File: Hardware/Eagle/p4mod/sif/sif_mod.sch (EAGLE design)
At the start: 29 parts

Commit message: Lowered values of the segment resistors for the Sif board.
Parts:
- R2, R3, R4, R5, R6, R7, R8: value 82 -> 75
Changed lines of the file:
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@@
 <part name="SUPPLY2" library="supply2" deviceset="GND" device=""/>
 <part name="SUPPLY3" library="supply2" deviceset="GND" device=""/>
-<part name="R2" library="resistor_mod" deviceset="R-EU_" device="R0402" value="82"/>
-<part name="R3" library="resistor_mod" deviceset="R-EU_" device="R0402" value="82"/>
-<part name="R4" library="resistor_mod" deviceset="R-EU_" device="R0402" value="82"/>
-<part name="R5" library="resistor_mod" deviceset="R-EU_" device="R0402" value="82"/>
-<part name="R6" library="resistor_mod" deviceset="R-EU_" device="R0402" value="82"/>
-<part name="R7" library="resistor_mod" deviceset="R-EU_" device="R0402" value="82"/>
-<part name="R8" library="resistor_mod" deviceset="R-EU_" device="R0402" value="82"/>
+<part name="R2" library="resistor_mod" deviceset="R-EU_" device="R0402" value="75"/>
+<part name="R3" library="resistor_mod" deviceset="R-EU_" device="R0402" value="75"/>
+<part name="R4" library="resistor_mod" deviceset="R-EU_" device="R0402" value="75"/>
+<part name="R5" library="resistor_mod" deviceset="R-EU_" device="R0402" value="75"/>
+<part name="R6" library="resistor_mod" deviceset="R-EU_" device="R0402" value="75"/>
+<part name="R7" library="resistor_mod" deviceset="R-EU_" device="R0402" value="75"/>
+<part name="R8" library="resistor_mod" deviceset="R-EU_" device="R0402" value="75"/>
 <part name="FRAME1" library="frames" deviceset="A4-SMALL-DOCFIELD" device="" value="Pulsar P4 Replacement Module"/>
 <part name="C4" library="resistor_mod" deviceset="C-EU" device="C0402K" value="12 pF"/>

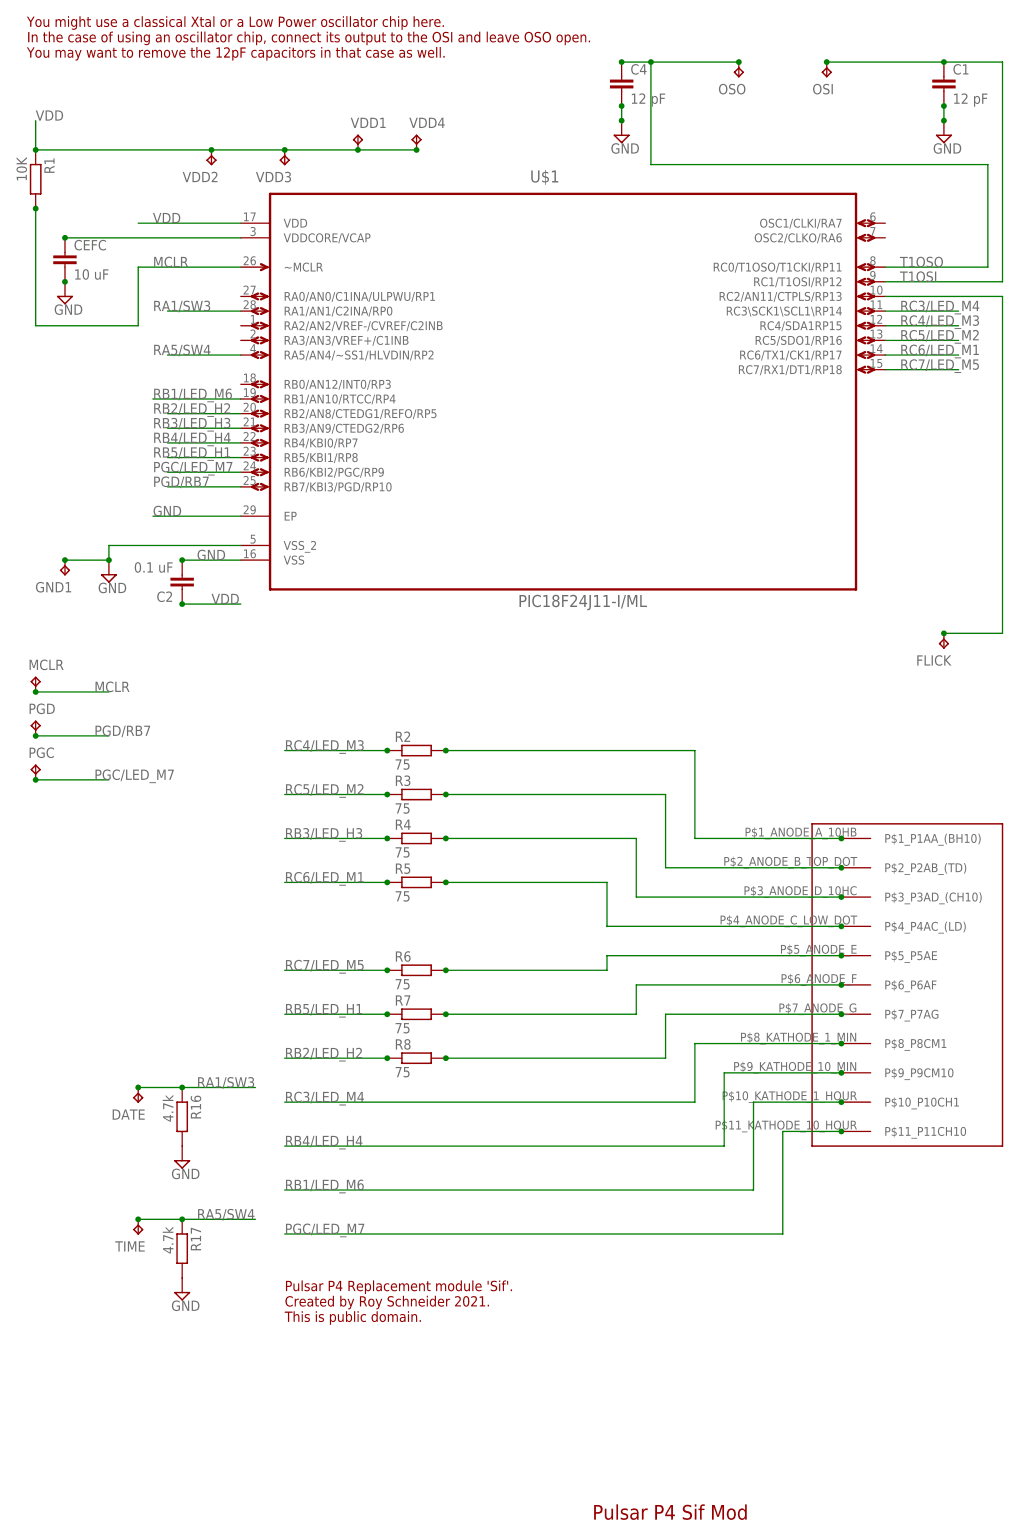
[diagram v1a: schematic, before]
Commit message: Upgraded Sif module to use nmos transistors for the common cathodes.
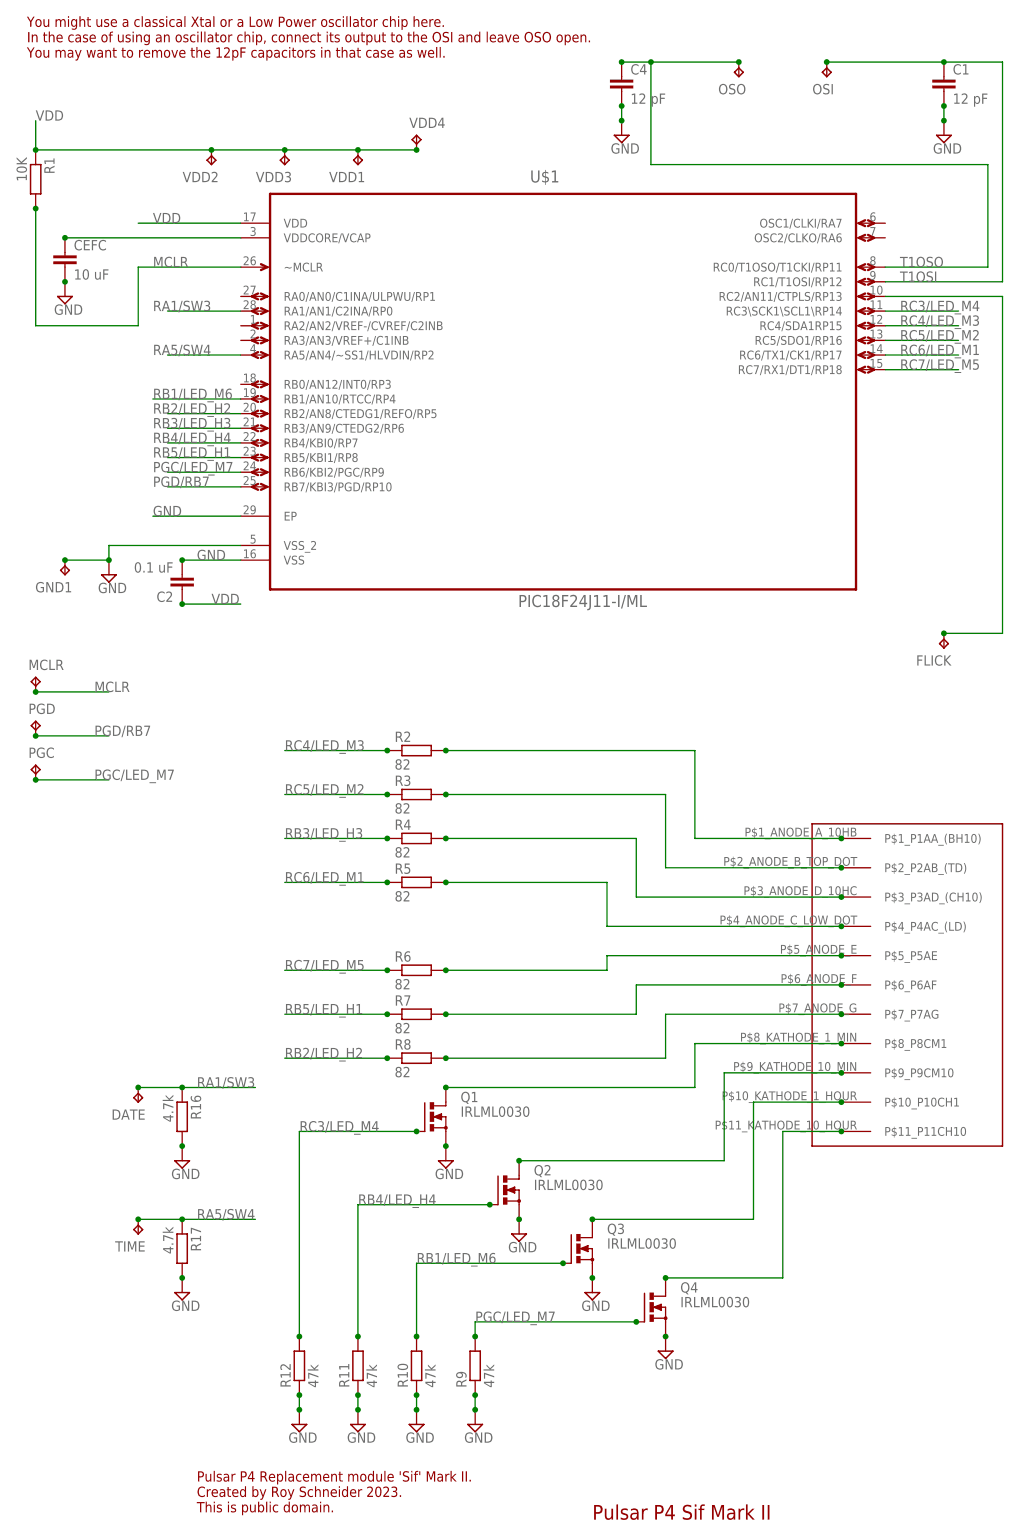
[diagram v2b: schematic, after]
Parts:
- added Q1, Q2, Q3, Q4: IRLML0030, irlml0030:IRLML0030
- added R10, R11, R12, R9: 47k, resistor_mod:R-EU_R0402
- R2, R3, R4, R5, R6, R7, R8: value 75 -> 82
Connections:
- new net N$11: Q2.D, U$2.P$9_P9CM10
- new net N$12: Q3.D, U$2.P$10_P10CH1
- new net N$13: Q4.D, U$2.P$11_P11CH10
- new net N$14: Q1.D, U$2.P$8_P8CM1
- net GND: now also Q1.S, Q2.S, Q3.S, Q4.S, R10.1, R11.1, R12.1, R9.1
- net PGC/LED_M7: now also Q4.G, R9.2; no longer U$2.P$11_P11CH10
- net RB1/LED_M6: now also Q3.G, R10.2; no longer U$2.P$10_P10CH1
- net RB4/LED_H4: now also Q2.G, R11.2; no longer U$2.P$9_P9CM10
- net RC3/LED_M4: now also Q1.G, R12.2; no longer U$2.P$8_P8CM1
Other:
- note added: "Pulsar P4 Replacement module 'Sif' Mark II. Created by Roy Schneider 2023. This is public domain."
- note added: "Pulsar P4 Sif Mark II"
- note removed: "Pulsar P4 Replacement module 'Sif'. Created by Roy Schneider 2021. This is public domain."
- note removed: "Pulsar P4 Sif Mod"
- moved on the sheet: VDD1

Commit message: Updated footprint of 10 uF ceramic cap to 0602.
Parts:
- CEFC: device resistor_mod:C-EUC0402K -> rcl:C-EUC0603
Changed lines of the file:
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@@
 <part name="R1" library="resistor_mod" deviceset="R-EU_" device="R0402" value="10K"/>
 <part name="C2" library="resistor_mod" deviceset="C-EU" device="C0402K" value="0.1 uF"/>
-<part name="CEFC" library="resistor_mod" deviceset="C-EU" device="C0402K" value="10 uF"/>
+<part name="CEFC" library="rcl" deviceset="C-EU" device="C0603" value="10 uF"/>
 <part name="SUPPLY2" library="supply2" deviceset="GND" device=""/>
 <part name="SUPPLY3" library="supply2" deviceset="GND" device=""/>

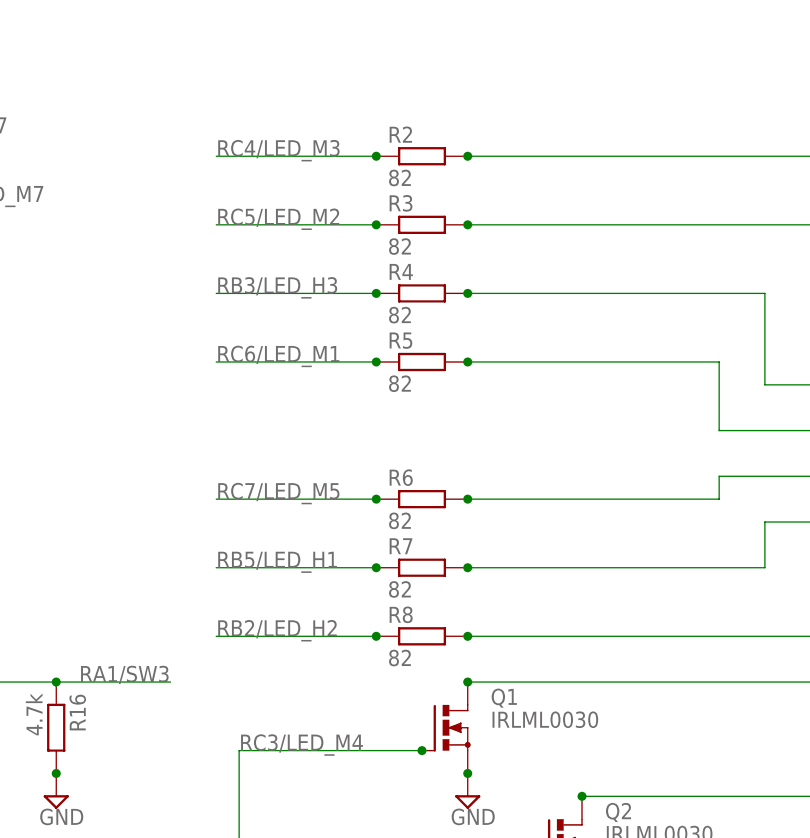
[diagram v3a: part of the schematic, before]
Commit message: Improved segment resistor values.
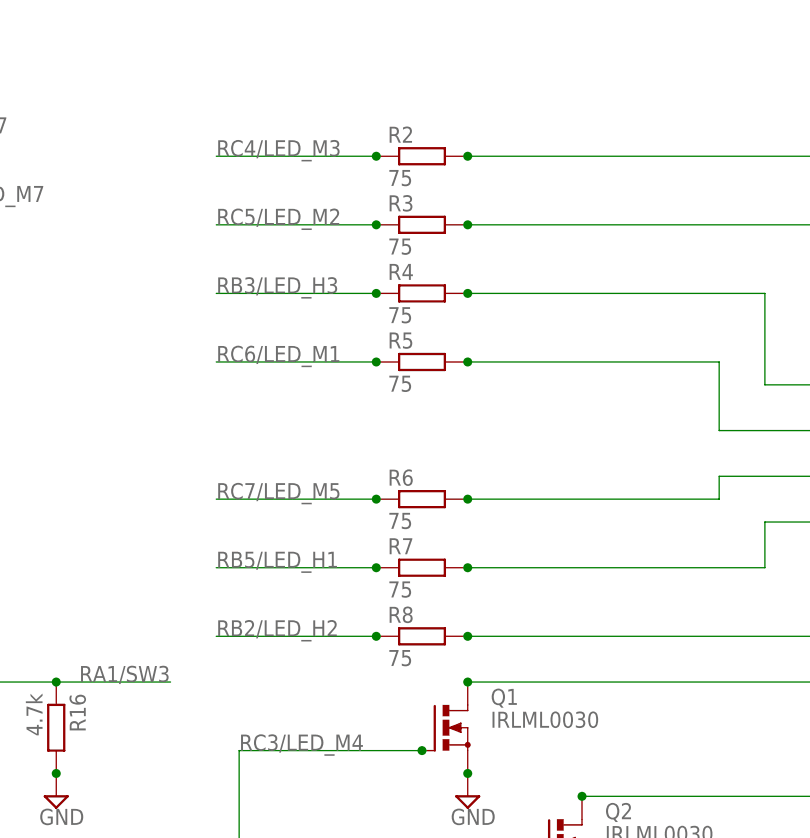
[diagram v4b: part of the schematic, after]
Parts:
- R2, R3, R4, R5, R6, R7, R8: value 82 -> 75
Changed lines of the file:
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@@
 <part name="SUPPLY2" library="supply2" deviceset="GND" device=""/>
 <part name="SUPPLY3" library="supply2" deviceset="GND" device=""/>
-<part name="R2" library="resistor_mod" deviceset="R-EU_" device="R0402" value="82"/>
-<part name="R3" library="resistor_mod" deviceset="R-EU_" device="R0402" value="82"/>
-<part name="R4" library="resistor_mod" deviceset="R-EU_" device="R0402" value="82"/>
-<part name="R5" library="resistor_mod" deviceset="R-EU_" device="R0402" value="82"/>
-<part name="R6" library="resistor_mod" deviceset="R-EU_" device="R0402" value="82"/>
-<part name="R7" library="resistor_mod" deviceset="R-EU_" device="R0402" value="82"/>
-<part name="R8" library="resistor_mod" deviceset="R-EU_" device="R0402" value="82"/>
+<part name="R2" library="resistor_mod" deviceset="R-EU_" device="R0402" value="75"/>
+<part name="R3" library="resistor_mod" deviceset="R-EU_" device="R0402" value="75"/>
+<part name="R4" library="resistor_mod" deviceset="R-EU_" device="R0402" value="75"/>
+<part name="R5" library="resistor_mod" deviceset="R-EU_" device="R0402" value="75"/>
+<part name="R6" library="resistor_mod" deviceset="R-EU_" device="R0402" value="75"/>
+<part name="R7" library="resistor_mod" deviceset="R-EU_" device="R0402" value="75"/>
+<part name="R8" library="resistor_mod" deviceset="R-EU_" device="R0402" value="75"/>
 <part name="FRAME1" library="frames" deviceset="A4-SMALL-DOCFIELD" device="" value="Pulsar P4 Replacement Module"/>
 <part name="C4" library="resistor_mod" deviceset="C-EU" device="C0402K" value="12 pF"/>
